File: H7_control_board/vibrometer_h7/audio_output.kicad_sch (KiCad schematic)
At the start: 0 parts

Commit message: working on getting ERC to run... almost there!
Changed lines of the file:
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@@
 	(generator_version "8.0")
 	(paper "A4")
-	(junction
-		(at 114.3 78.74)
-		(diameter 0)
-		(color 0 0 0 0)
-	)
-	(wire
-		(pts
-			(xy 114.3 78.74) (xy 114.3 76.2)
-		)
-		(stroke
-			(width 0)
-			(type default)
-		)
-	)
 	(wire
 		(pts
@@
 	(wire
 		(pts
-			(xy 114.3 81.28) (xy 114.3 78.74)
+			(xy 129.54 76.2) (xy 129.54 78.74)
 		)
 		(stroke
@@
 	(wire
 		(pts
-			(xy 88.9 76.2) (xy 114.3 76.2)
+			(xy 88.9 76.2) (xy 129.54 76.2)
 		)
 		(stroke
@@
 		)
 	)
-	(symbol
-		(lib_id "power:GND")
-		(at 114.3 81.28 0)
-		(unit 1)
-		(exclude_from_sim no)
-		(in_bom yes)
-		(on_board yes)
-		(dnp no)
-		(fields_autoplaced yes)
-		(property "Reference" "#PWR067"
-			(at 114.3 87.63 0)
-			(effects
-				(font
-					(size 1.27 1.27)
-				)
-				(hide yes)
-			)
-		)
-		(property "Value" "GND"
-			(at 114.3 86.36 0)
-			(effects
-				(font
-					(size 1.27 1.27)
-				)
-				(hide yes)
-			)
-		)
-		(property "Footprint" ""
-			(at 114.3 81.28 0)
-			(effects
-				(font
-					(size 1.27 1.27)
-				)
-				(hide yes)
-			)
-		)
-		(property "Datasheet" ""
-			(at 114.3 81.28 0)
-			(effects
-				(font
-					(size 1.27 1.27)
-				)
-				(hide yes)
-			)
-		)
-		(property "Description" "Power symbol creates a global label with name \"GND\" , ground"
-			(at 114.3 81.28 0)
-			(effects
-				(font
-					(size 1.27 1.27)
-				)
-				(hide yes)
-			)
-		)
-		(pin "1"
-		)
-		(instances
-			(project ""
-				(path "/18de6987-156a-4b34-871e-cbbe1d261986/baa2f8d8-a947-4685-9d57-97bd2d075f25"
-					(reference "#PWR067")
-					(unit 1)
-				)
-			)
-		)
-	)

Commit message: worked on audio output stuff, cleaned schematic
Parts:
- added C10, C4, C6, C7, C8, C9: C_Small, symbol Device:C_Small
- added J2: AudioJack3, symbol Connector_Audio:AudioJack3
- added R1, R2, R3, R4: R_Small_US, symbol Device:R_Small_US
- added U5: TPA6132A2RTE, Package_DFN_QFN:WQFN-16-1EP_3x3mm_P0.5mm_EP1.6x1.6mm_ThermalVias, symbol Amplifier_Audio:TPA6132A2RTE
- added U6: TPA6111A2, Package_SO:HVSSOP-8-1EP_3x3mm_P0.65mm_EP1.57x1.89mm, symbol vibrometer_project:TPA6110A2DGN
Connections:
- net DAC_OUTA: now also C4.1
- net DAC_OUTB: now also C6.1
- new net: C7.1, R3.2, U6.7 (VO1)
- new net: C7.2, J2.R
- new net: C8.2, J2.T
- new net: C6.2, R2.1
- new net: R1.2, R3.1, U6.8 (IN1-)
- new net: C4.2, R1.1
- new net: R2.2, R4.1, U6.4 (IN2-)
- new net: C8.1, R4.2, U6.5 (VO2)
- new net: C9.2, U6.1 (BYPASS)
- new net +3V3A: C10.1, U6.6 (VDD)
- new net GND: C10.2, C9.1, J2.S, U6.2 (GND), U6.9 (GND)
- new net MUTE_SIGNAL: U6.3 (~{SHDN})
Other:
- note added: "https://www.analogfilters.com/high-quality-reconstruction-lowpass-filter-for-digital-audio/"
- note added: "https://www.eevblog.com/forum/beginners/connecting-microcontroller-dac-to-speakers/"
- note added: "https://www.lcsc.com/datasheet/lcsc_datasheet_1808280152_Diodes-Incorporated-PAM8908JER_C33233.pdf"
- note added: "https://www.lcsc.com/datasheet/lcsc_datasheet_1809121817_Texas-Instruments-TPA6138A2PWR_C183097.pdf"
- note added: "https://www.lcsc.com/datasheet/lcsc_datasheet_2003172206_Texas-Instruments-TPA6111A2DR_C497472.pdf"
- note added: "https://www.st.com/resource/en/application_note/an3126-audio-and-waveform-generation-using-the-dac-in-stm32-products-stmicroelectronics.pdf"
- note added: "https://www.ti.com/lit/an/slea048/slea048.pdf?ts=1722405290905"

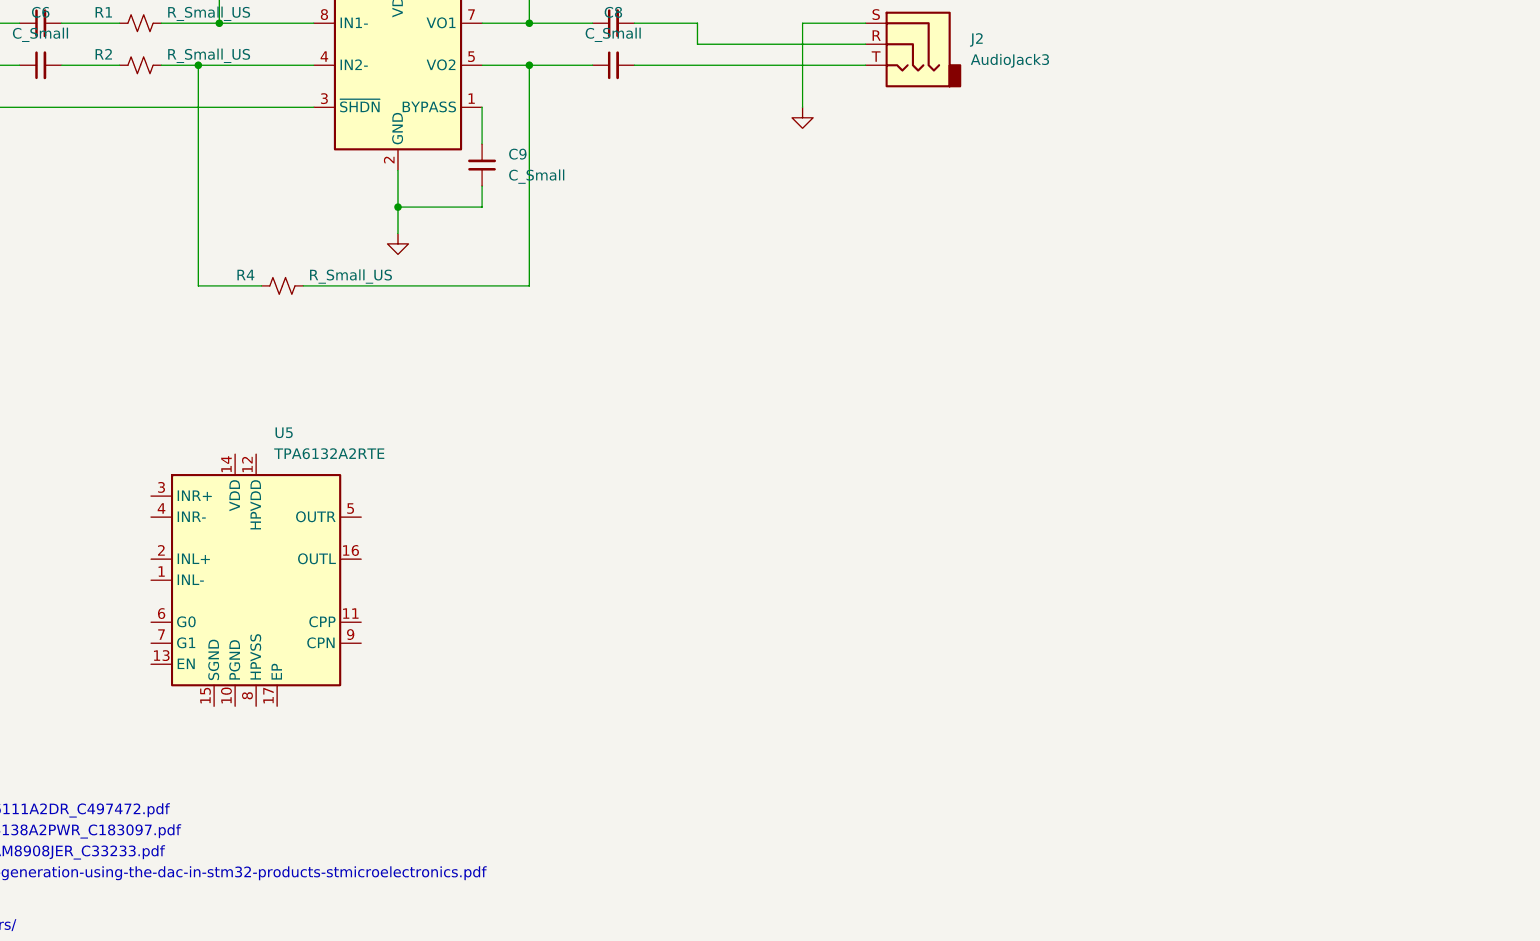
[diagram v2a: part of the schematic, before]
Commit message: met with john to go over schematic. made changes, got rid of some leds...
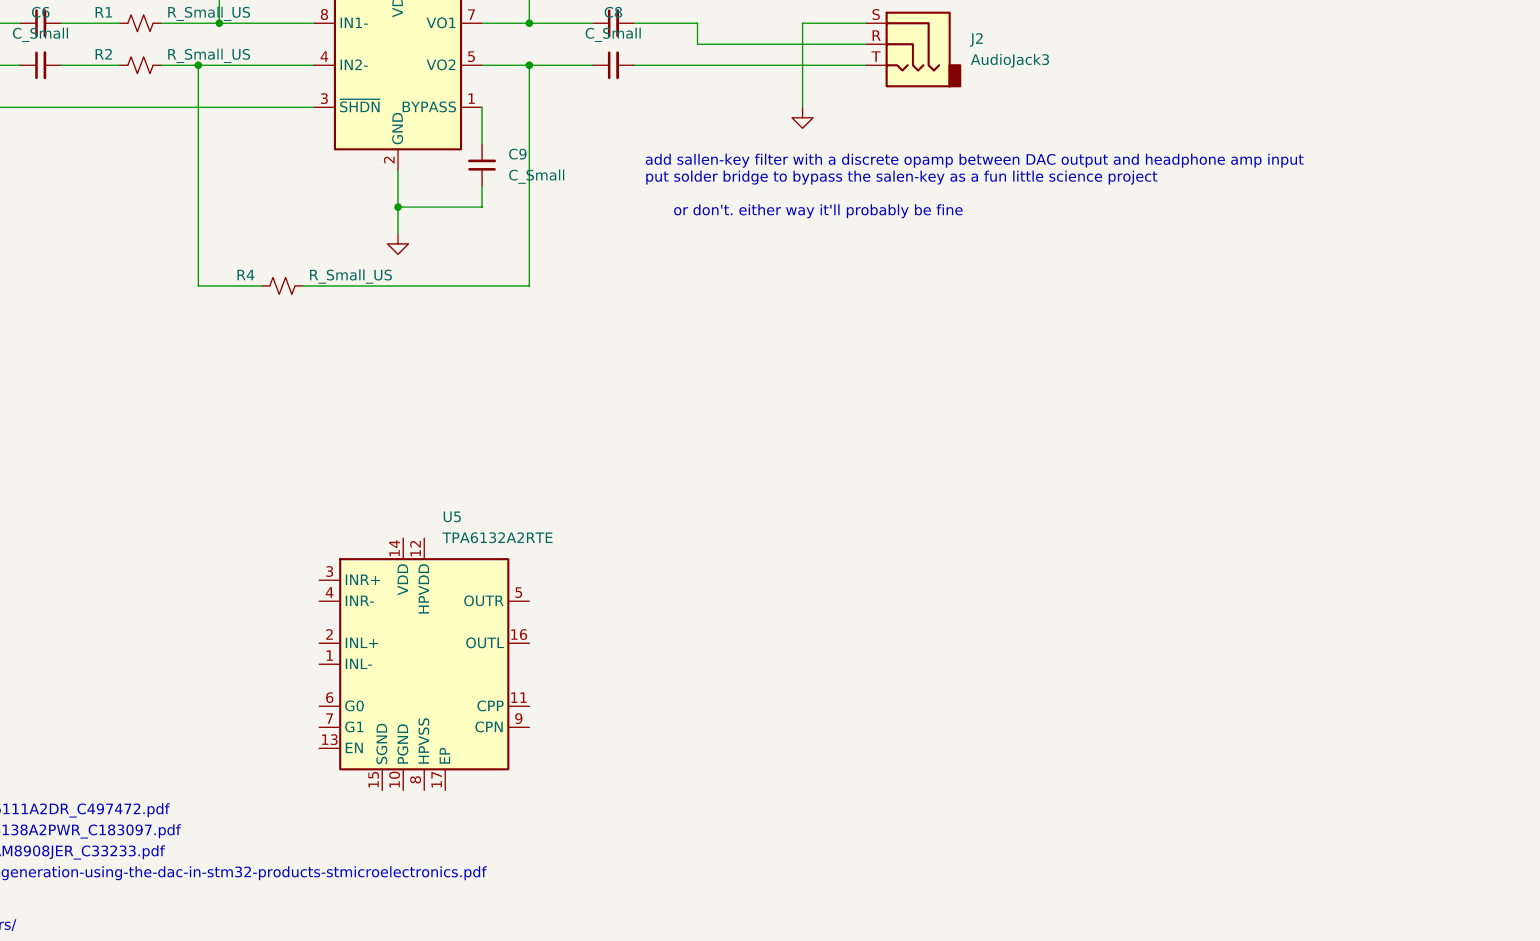
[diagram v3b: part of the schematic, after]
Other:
- note added: "add sallen-key filter with a discrete opamp between DAC output and headphone amp input put solder bridge to bypass the salen-key as a fun little science project"
- note added: "or don't. either way it'll probably be fine"
- moved on the sheet: U5
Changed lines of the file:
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@@
+		)
+	)
+	(text "or don't. either way it'll probably be fine"
+		(exclude_from_sim no)
+		(at 201.295 99.06 0)
+		(effects
+			(font
+				(size 1.27 1.27)
+			)
+		)
+	)
+	(text "add sallen-key filter with a discrete opamp between DAC output and headphone amp input\nput solder bridge to bypass the salen-key as a fun little science project"
+		(exclude_from_sim no)
+		(at 180.34 93.98 0)
+		(effects
+			(font
+				(size 1.27 1.27)
+			)
+			(justify left)
 		)
 	)
@@
 	(symbol
 		(lib_id "Amplifier_Audio:TPA6132A2RTE")
-		(at 133.35 143.51 0)
+		(at 153.67 153.67 0)
 		(unit 1)
 		(exclude_from_sim no)
@@
 		(fields_autoplaced yes)
 		(property "Reference" "U5"
-			(at 135.5441 125.73 0)
+			(at 155.8641 135.89 0)
 			(effects
 				(font
@@
 		)
 		(property "Value" "TPA6132A2RTE"
-			(at 135.5441 128.27 0)
+			(at 155.8641 138.43 0)
 			(effects
 				(font
@@
 		)
 		(property "Footprint" "Package_DFN_QFN:WQFN-16-1EP_3x3mm_P0.5mm_EP1.6x1.6mm_ThermalVias"
-			(at 135.89 157.48 0)
+			(at 156.21 167.64 0)
 			(effects
 				(font
@@
 		)
 		(property "Datasheet" "https://www.ti.com/lit/ds/symlink/tpa6132a2.pdf"
-			(at 125.73 129.54 0)
+			(at 146.05 139.7 0)
 			(effects
 				(font
@@
 		)
 		(property "Description" "25mW, Stereo, DirectPath Audio Amplifier, WQFN-16"
-			(at 133.35 143.51 0)
-			(effects
-				(font
+			(at 153.67 153.67 0)
+			(effects
+				(font

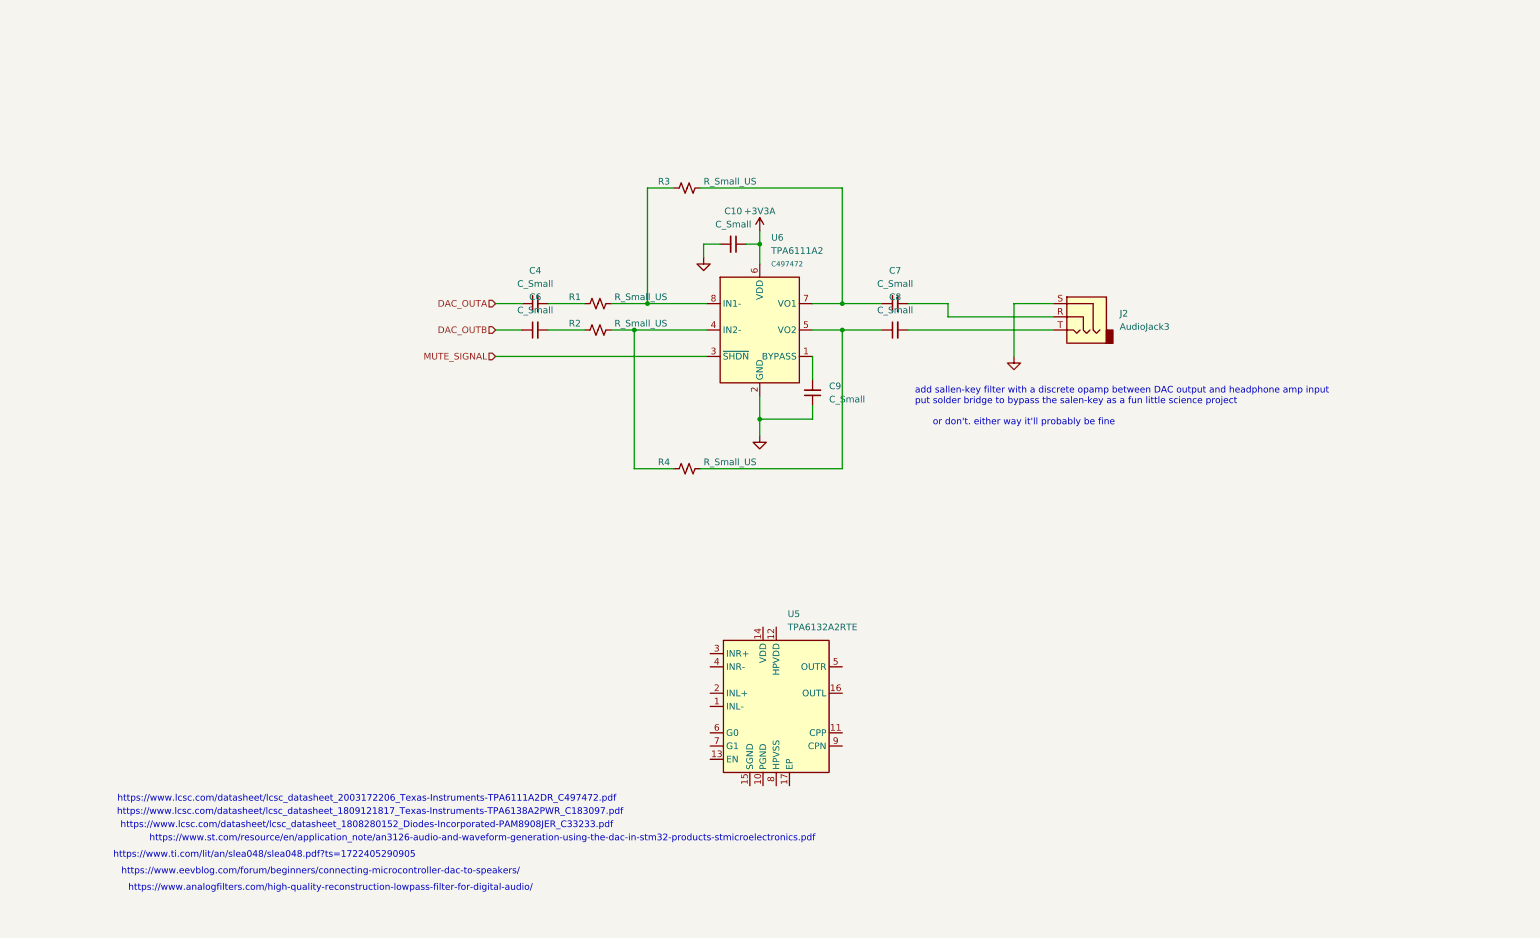
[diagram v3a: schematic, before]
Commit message: updated audio filter circuit
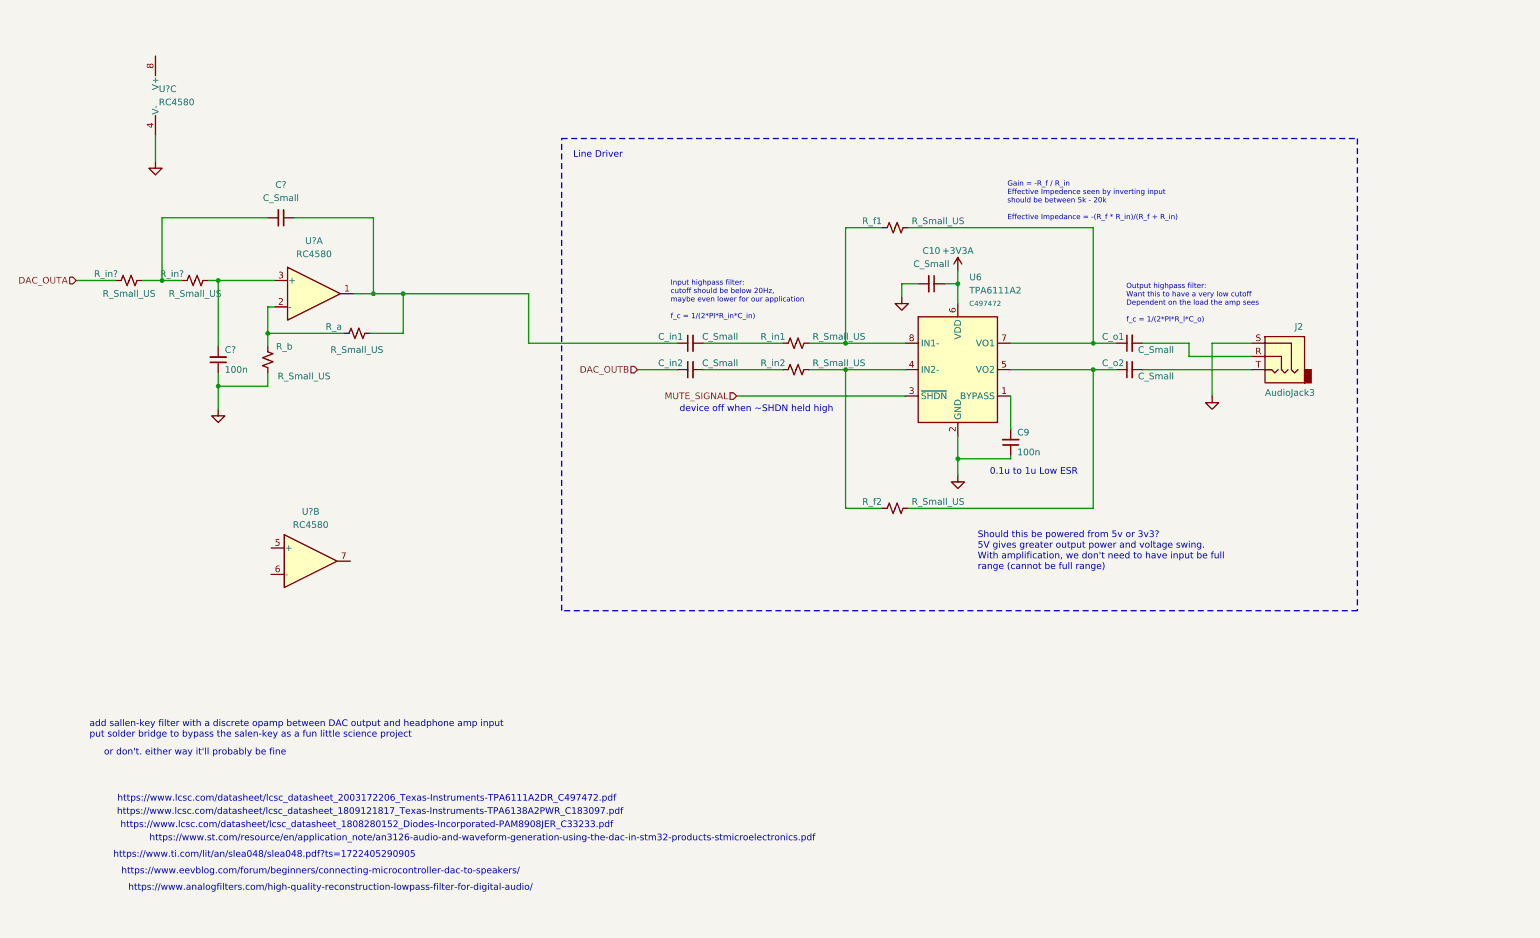
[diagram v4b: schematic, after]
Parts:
- removed U5: TPA6132A2RTE, Package_DFN_QFN:WQFN-16-1EP_3x3mm_P0.5mm_EP1.6x1.6mm_ThermalVias, symbol Amplifier_Audio:TPA6132A2RTE
- added C?: C_Small, symbol Device:C_Small
- added C?: 100n, symbol Device:C_Small
- added R_a, R_b, R_in? (x2): R_Small_US, symbol Device:R_Small_US
- added U? (x3): RC4580, symbol Amplifier_Operational:RC4580
- C9: value C_Small -> 100n
- renumbered C4 to C_in1, C6 to C_in2, C7 to C_o1, C8 to C_o2, R3 to R_f1, R4 to R_f2, R1 to R_in1, R2 to R_in2
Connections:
- net DAC_OUTA: now also R_in?.1; no longer C_in1.1
- net GND: now also C?.1, R_b.1, U?.4 (V-)
- new net: R_a.1, R_b.2, U?.2 (-)
- new net: C?.1, C_in1.1, R_a.2, U?.1
- new net: C?.2, R_in?.2, U?.3 (+)
- new net: C?.2, R_in?.1, R_in?.2
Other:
- note added: "0.1u to 1u Low ESR"
- note added: "Gain = -R_f / R_in Effective Impedence seen by inverting input should be between 5k - 20k Effective Impedance = -(R_f * R_in)/(R_f + R_in)"
- note added: "Input highpass filter: cutoff should be below 20Hz, maybe even lower for our application f_c = 1/(2*PI*R_in*C_in)"
- note added: "Line Driver"
- note added: "Output highpass filter: Want this to have a very low cutoff Dependent on the load the amp sees f_c = 1/(2*PI*R_l*C_o)"
- note added: "Should this be powered from 5v or 3v3? 5V gives greater output power and voltage swing. With amplification, we don't need to have input be full range (cannot be full range)"
- note added: "device off when ~SHDN held high"
- moved on the sheet: C10, C9, C_in1, C_in2, C_o1, C_o2, J2, R_f1, R_f2, R_in1, R_in2, U6

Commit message: started part selection
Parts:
- C10, C9, C? (x2), C_in1, C_in2, C_o1, C_o2: footprint (none) -> Capacitor_SMD:C_0603_1608Metric
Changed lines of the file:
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@@
 			)
 		)
-		(property "Footprint" ""
+		(property "Footprint" "Capacitor_SMD:C_0603_1608Metric"
 			(at 221.615 83.82 0)
 			(effects
@@
 			)
 		)
-		(property "Footprint" ""
+		(property "Footprint" "Capacitor_SMD:C_0603_1608Metric"
 			(at 137.16 88.9 0)
 			(effects
@@
 			)
 		)
-		(property "Footprint" ""
+		(property "Footprint" "Capacitor_SMD:C_0603_1608Metric"
 			(at 137.16 83.82 0)
 			(effects
@@
 			)
 		)
-		(property "Footprint" ""
+		(property "Footprint" "Capacitor_SMD:C_0603_1608Metric"
 			(at 221.615 88.9 0)
 			(effects
@@
 			)
 		)
-		(property "Footprint" ""
+		(property "Footprint" "Capacitor_SMD:C_0603_1608Metric"
 			(at 198.755 102.87 0)
 			(effects
@@
 			)
 		)
-		(property "Footprint" ""
+		(property "Footprint" "Capacitor_SMD:C_0603_1608Metric"
 			(at 58.42 59.69 0)
 			(effects
@@
 			)
 		)
-		(property "Footprint" ""
+		(property "Footprint" "Capacitor_SMD:C_0603_1608Metric"
 			(at 183.515 72.39 0)
 			(effects
@@
 			)
 		)
-		(property "Footprint" ""
+		(property "Footprint" "Capacitor_SMD:C_0603_1608Metric"
 			(at 46.355 86.995 0)
 			(effects
